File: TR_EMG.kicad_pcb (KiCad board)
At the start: 2 copper layers, 118 parts, among them J1 1727230, J2 1727230, J3 1844236, J4 MJ-3523-SMT-TR, J5 MJ-3523-SMT-TR, J6 MJ-3523-SMT-TR, J7 MJ-3523-SMT-TR, U1 ADS1115IDGSR, U101 INA115BU, U111 LT1169CS8-PBF, U112 LT1169CS8-PBF, U201 INA115BU, U211 LT1169CS8-PBF, U212 LT1169CS8-PBF, U301 INA115BU, U311 LT1169CS8-PBF, U312 LT1169CS8-PBF, U401 INA115BU, U411 LT1169CS8-PBF, U412 LT1169CS8-PBF

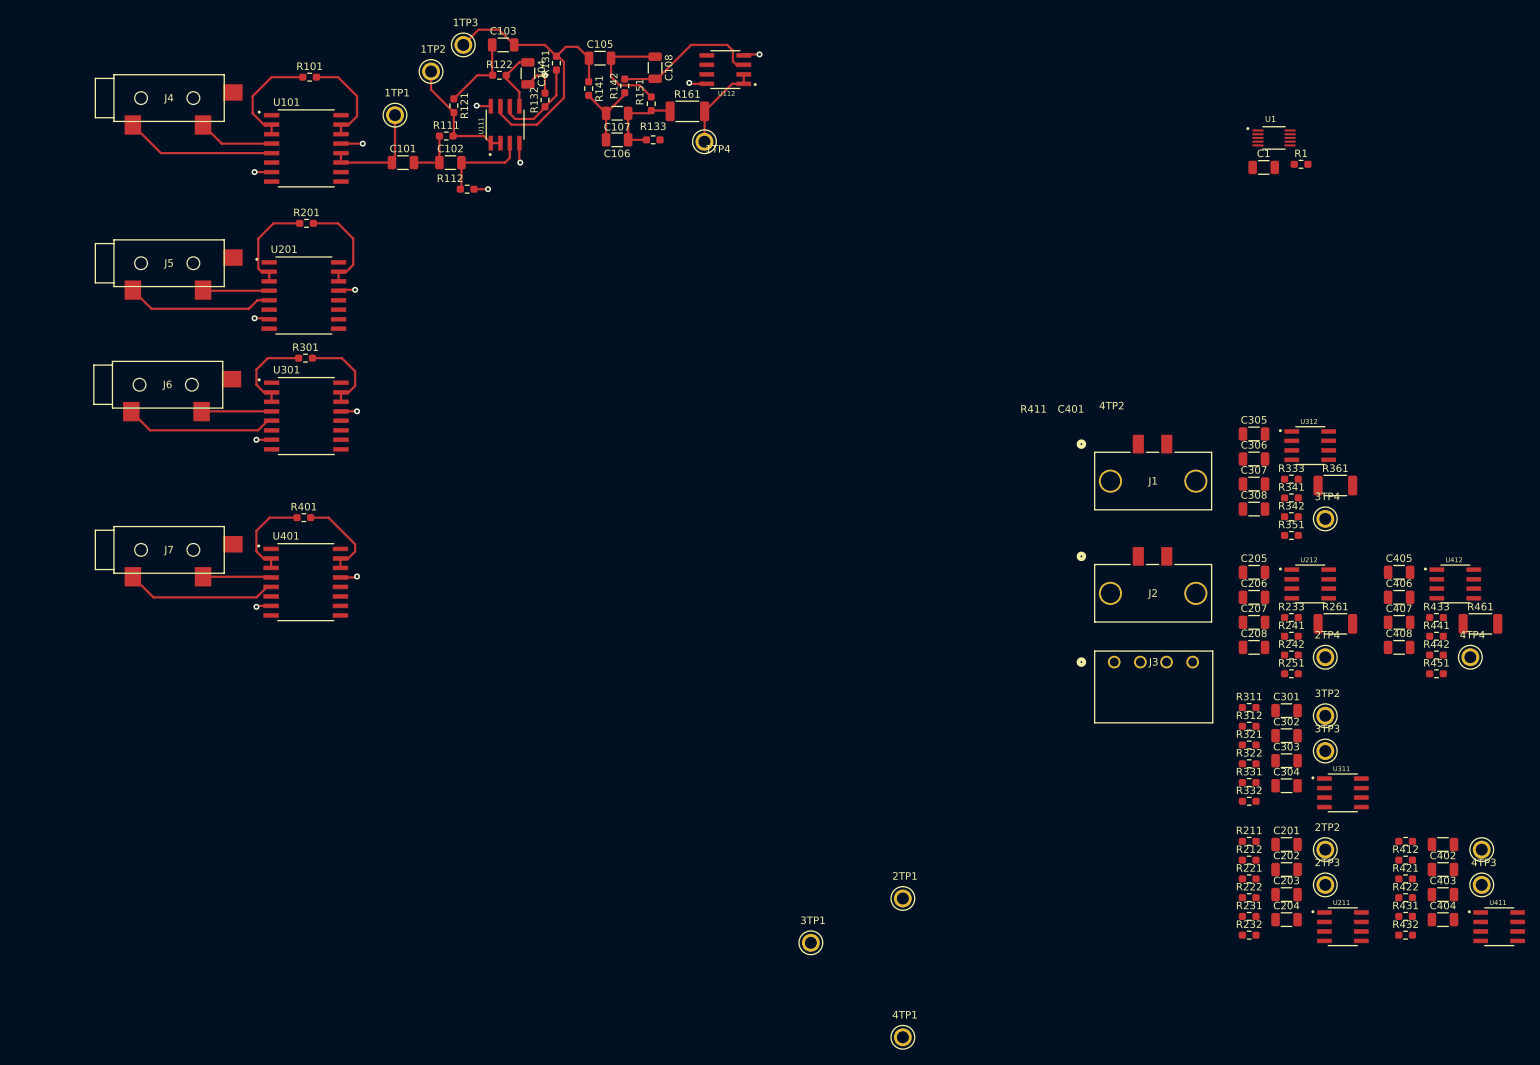
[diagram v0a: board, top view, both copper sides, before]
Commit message: finished majority of layout, pcb expanded to four copper layers to accomadate power planes
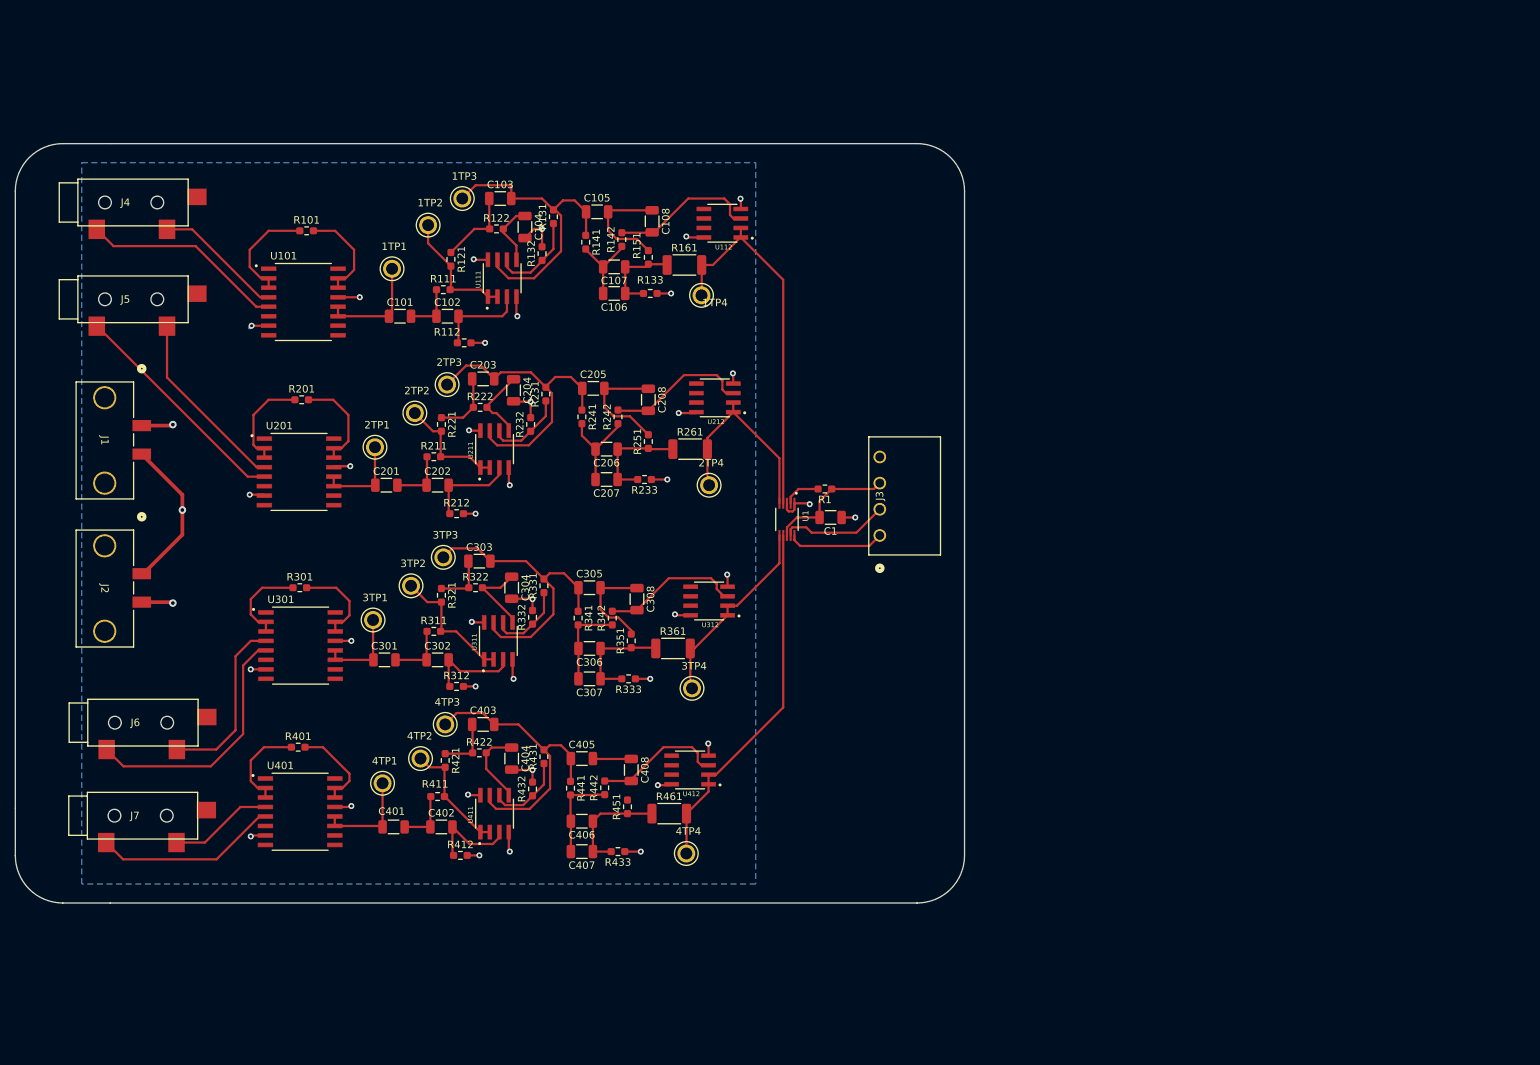
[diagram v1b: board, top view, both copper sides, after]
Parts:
- moved 4TP2 142.5 mm to (136.8, 120.4)
- moved C401 140.4 mm to (133.2, 129.5)
- moved 4TP3 140.3 mm to (140.1, 115.8)
- moved U411 135.3 mm to (146.7, 127.7), turned to 90 degrees
- moved 2TP3 135.2 mm to (140.3, 70.3)
- moved 2TP2 135.1 mm to (136.0, 74.1)
- moved C402 134.1 mm to (139.6, 129.5)
- moved J1 133.4 mm to (99.5, 75.8), turned to -90 degrees
- moved J2 133.4 mm to (99.5, 95.6), turned to -90 degrees
- moved C403 130.4 mm to (145.1, 115.8)
- moved U211 130.2 mm to (146.7, 79.0), turned to 90 degrees
- moved C201 129.7 mm to (132.2, 83.8)
- moved R411 129.7 mm to (139.1, 125.5)
- moved R421 129.5 mm to (140.1, 120.6), turned to -90 degrees
- moved C203 127.7 mm to (145.1, 69.6)
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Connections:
- J3 pad 1: /ADC/Power -> /ADC/SCL
- J3 pad 2: GNDD -> /ADC/SDA
- J3 pad 3: /ADC/SDA -> /ADC/Power
- J3 pad 4: /ADC/SCL -> GNDD
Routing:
- net /ADC/AIN3: track 0.00 -> 48.5 mm
- net GNDA: track 7.06 -> 53.9 mm, vias 2 -> 13
- net /Filter2/2nd Band Pass Filter (5 - 500 Hz)/Vout: track 0.00 -> 41.2 mm
- net /Filter3/2nd Band Pass Filter (5 - 500 Hz)/Vout: track 0.00 -> 40.5 mm
- net /Filter4/2nd Band Pass Filter (5 - 500 Hz)/Vout: track 0.00 -> 40.0 mm
- net /ADC/AIN0: track 12.1 -> 50.0 mm
- net /ADC/AIN1: track 0.00 -> 27.3 mm
- net /ADC/AIN2: track 0.00 -> 26.5 mm
- net Net-(U212-+INA): track 0.00 -> 19.1 mm
- net Net-(U312-+INA): track 0.00 -> 18.7 mm
- net Net-(U412-+INA): track 0.00 -> 17.6 mm
- net Net-(U311--INA): track 0.00 -> 17.6 mm
- net /ADC/Power: track 0.00 -> 17.2 mm
- net V-: track 13.2 -> 29.5 mm, vias 6 -> 13
- net Vin-(2): track 8.88 -> 24.9 mm
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- added copper zone on In2.Cu, net /ADC/Power
- added copper zone on In1.Cu, net GNDA
- added copper zone on In1.Cu, net GNDD
- added copper zone on In2.Cu, net V+
- added copper zone on B.Cu, net V-
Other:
- board outline added: 127 x 101.6 mm
- copper layers 2 -> 4

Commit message: Final touches to silkscreen on pcb, DRC check still needed
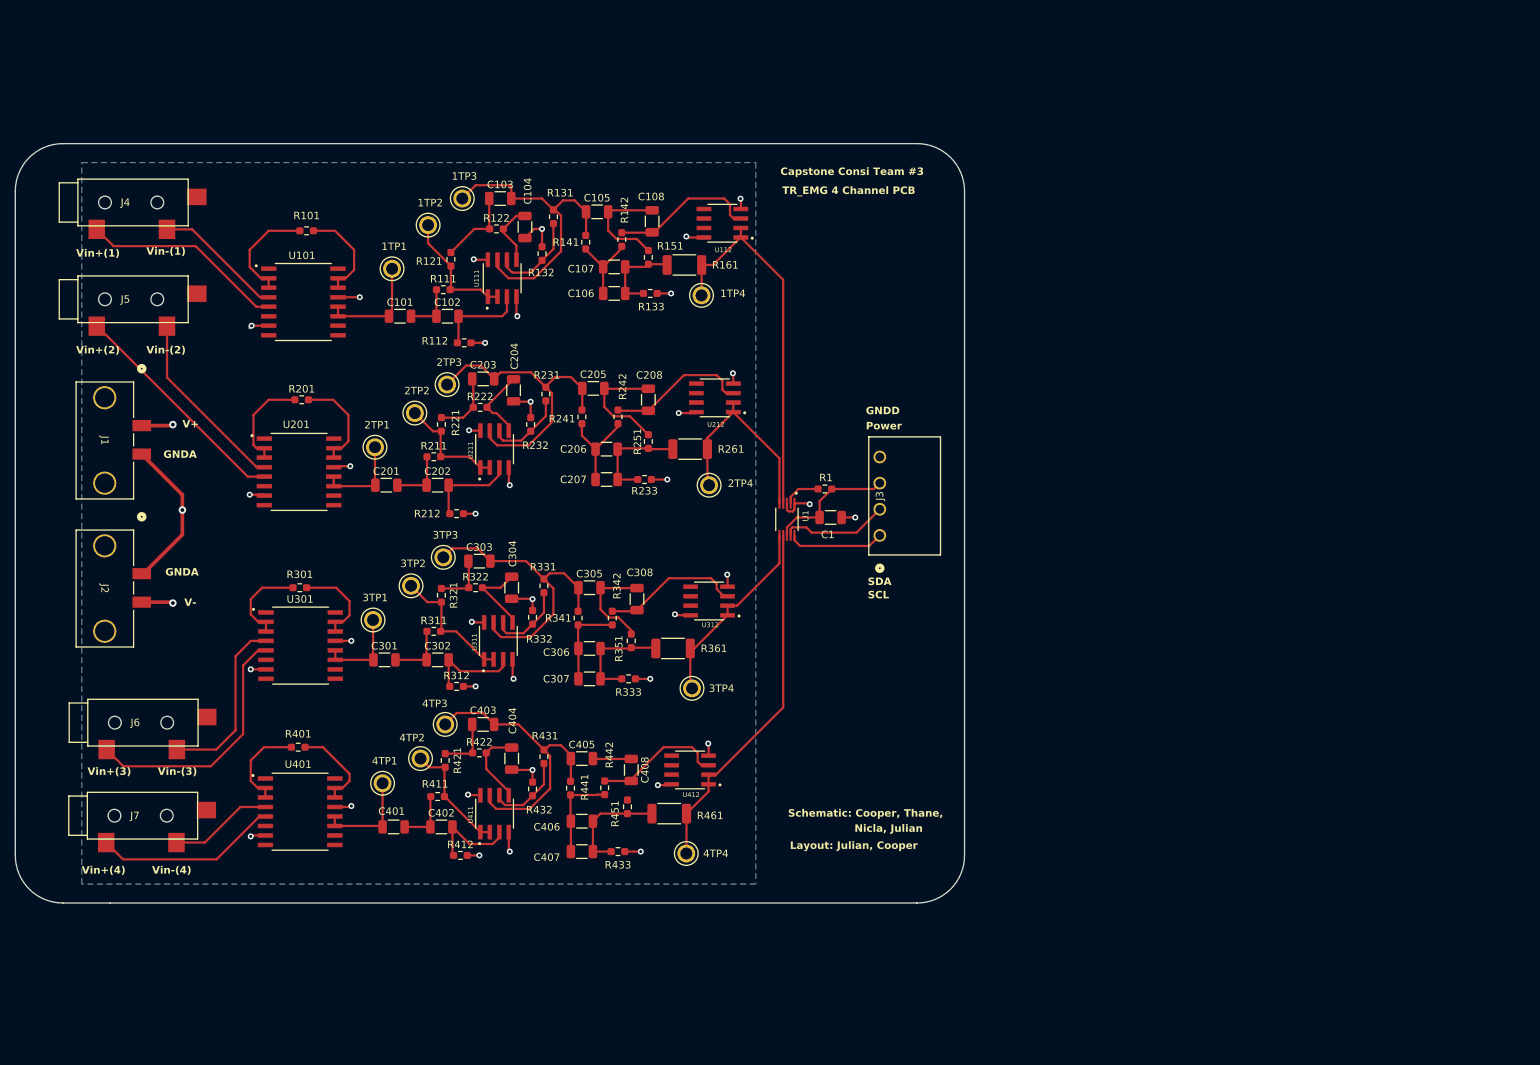
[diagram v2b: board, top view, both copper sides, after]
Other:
- board text added: "Capstone Consi Team #3"
- board text added: "GNDA"
- board text added: "GNDD"
- board text added: "Layout: Julian, Cooper"
- board text added: "Nicla, Julian"
- board text added: "Power"
- board text added: "SCL"
- board text added: "SDA"
- board text added: "Schematic: Cooper, Thane,"
- board text added: "TR_EMG 4 Channel PCB"
- board text added: "V+"
- board text added: "V-"
- board text added: "Vin+(1)"
- board text added: "Vin+(2)"
- board text added: "Vin+(3)"
- board text added: "Vin+(4)"
- board text added: "Vin-(1)"
- board text added: "Vin-(2)"
- board text added: "Vin-(3)"
- board text added: "Vin-(4)"

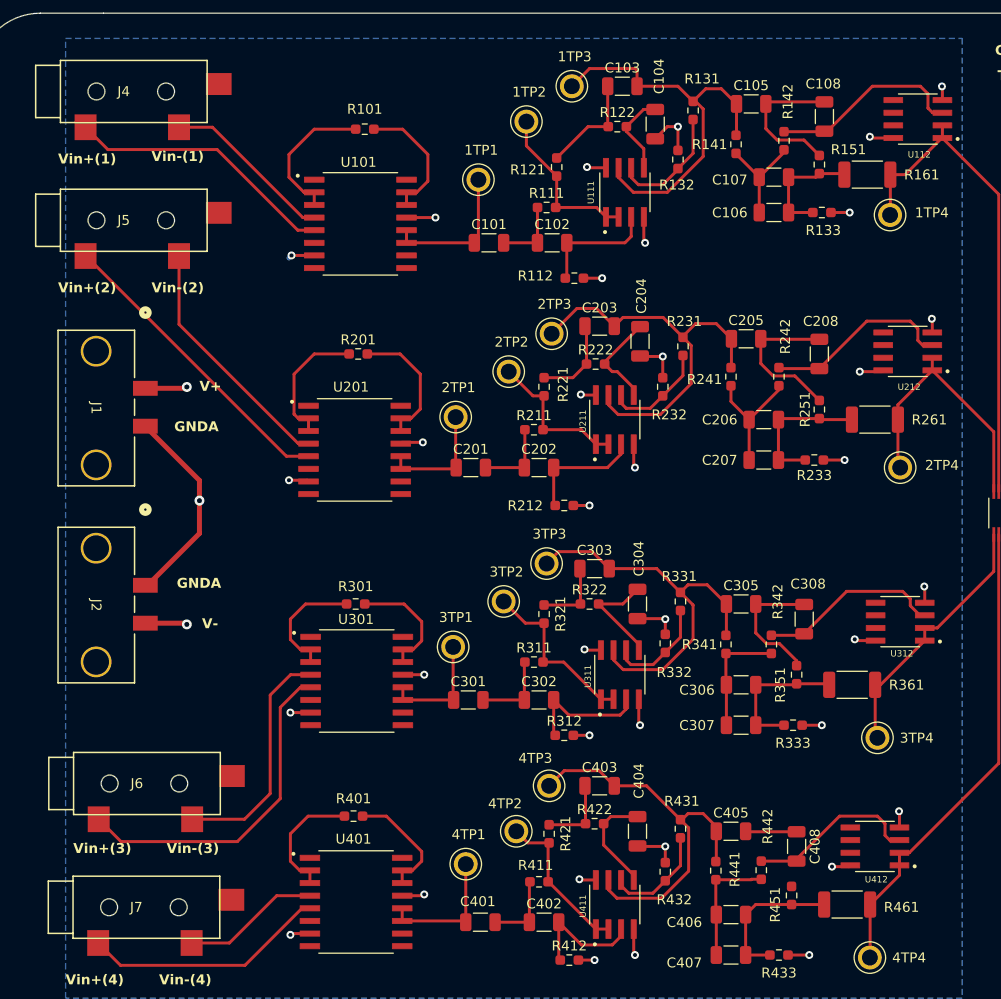
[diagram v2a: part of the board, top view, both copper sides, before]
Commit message: modified footprints and IC silkscreen refereence designators to comply with DRC checks
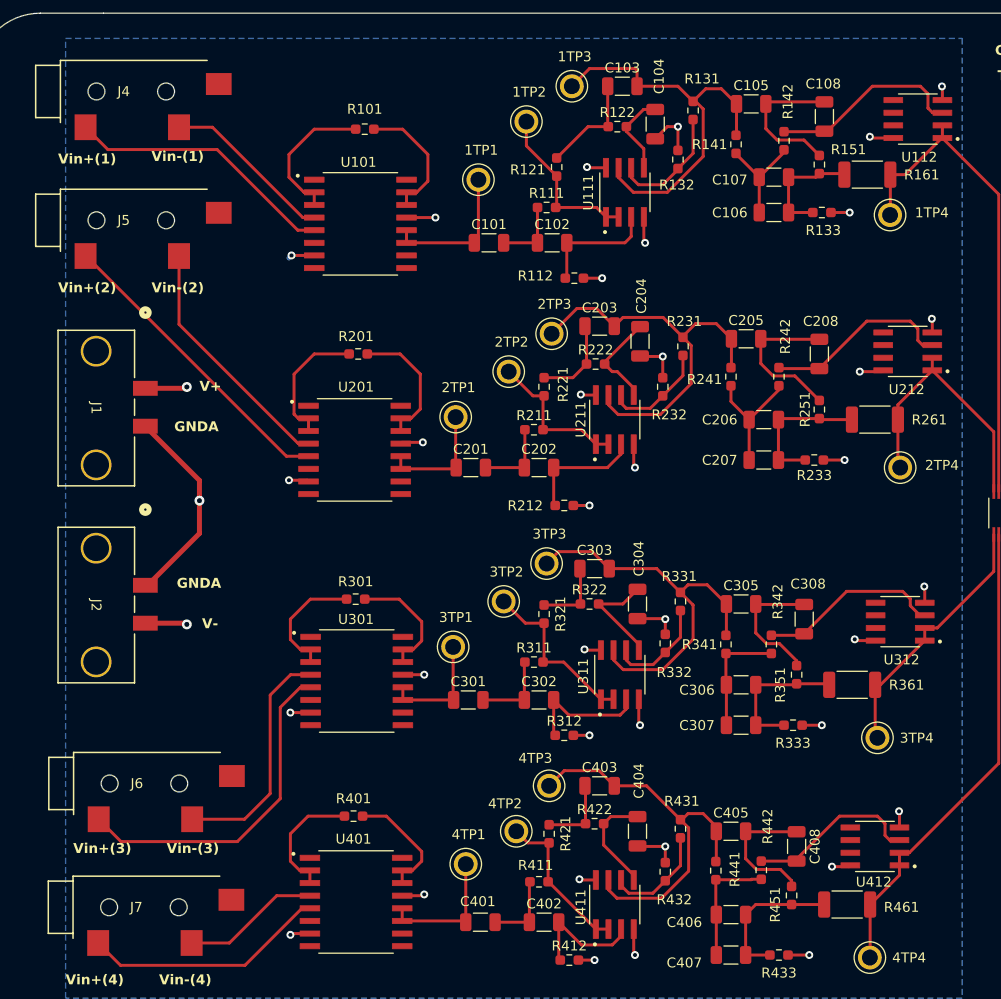
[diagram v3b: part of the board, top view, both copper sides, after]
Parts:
- moved R301 0.49 mm to (120.6, 97.0)
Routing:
- net Net-(C405-Pad2): track 5.15 -> 14.0 mm
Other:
- rule solder_mask_min_width: 0.1 -> 0.05

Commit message: DRC check passed, but ADC/ADS footprint needs to be checked for JLCPCB compatability (pads may be too close together)
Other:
- rule solder_mask_min_width: 0.05 -> 0.04
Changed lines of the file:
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@@
     )
     (pad_to_mask_clearance 0.04)
-    (solder_mask_min_width 0.05)
+    (solder_mask_min_width 0.04)
+    (allow_soldermask_bridges_in_footprints yes)
     (pcbplotparams
       (layerselection 0x00010fc_ffffffff)
